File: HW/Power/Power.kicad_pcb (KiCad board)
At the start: 2 copper layers, 22 x 55 mm, 7 parts, among them J1 Source, J2 Battery, U1 L7805

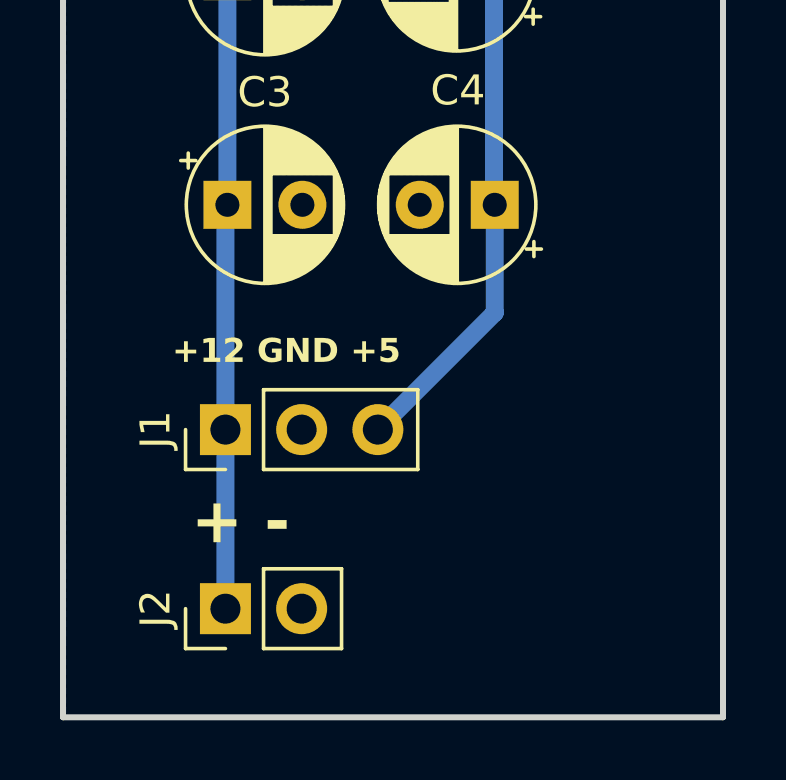
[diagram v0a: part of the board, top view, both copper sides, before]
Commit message: PCB's OK: power, H Bridge driver
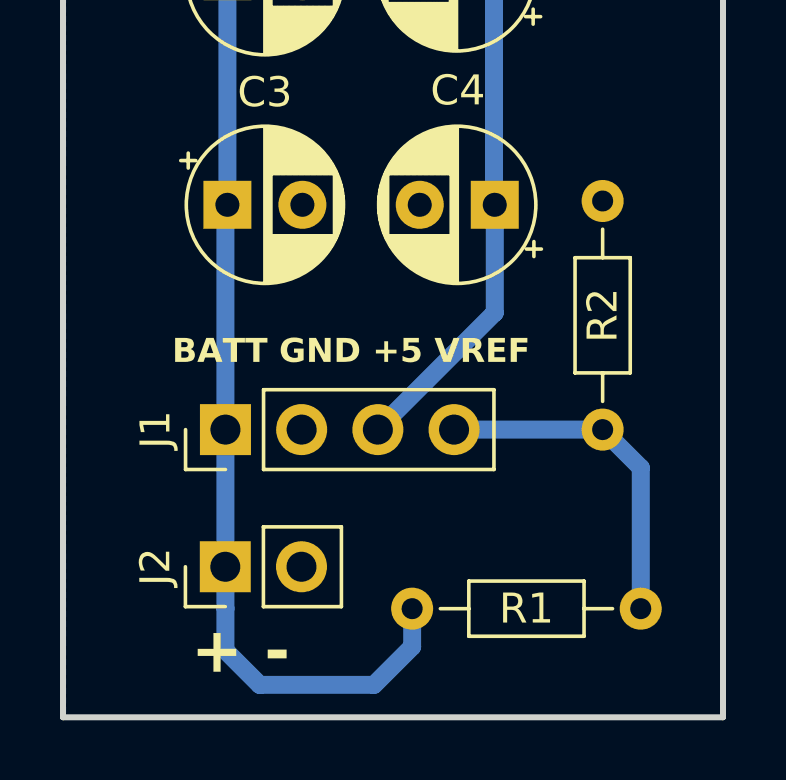
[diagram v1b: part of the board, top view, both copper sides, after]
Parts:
- added R1: 100k, Resistor_THT:R_Axial_DIN0204_L3.6mm_D1.6mm_P7.62mm_Horizontal, F.Cu at (151.6, 111.4)
- added R2: 100k, Resistor_THT:R_Axial_DIN0204_L3.6mm_D1.6mm_P7.62mm_Horizontal, F.Cu at (158.0, 105.4)
- J1: footprint Connector_PinHeader_2.54mm:PinHeader_1x03_P2.54mm_Vertical -> Connector_PinHeader_2.54mm:PinHeader_1x04_P2.54mm_Vertical
- moved J2 1.40 mm to (145.4, 110.0)
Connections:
- net +12V renamed +BATT
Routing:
- net VDD: track 0.00 -> 11.4 mm
- net +BATT: track 28.5 -> 38.4 mm
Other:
- board text added: "BATT GND +5 VREF"
- board text removed: "+12 GND +5"
